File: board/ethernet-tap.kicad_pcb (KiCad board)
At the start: 4 copper layers, 399 parts, among them J1 BARREL_JACK, J10 XILINX_JTAG, J2 BEL_FUSE_0826-1G1T-23-F, J3 JUMPER_0402_SPDT, J4 JUMPER_0402_SPDT, J5 RJ45, J6 BEL_FUSE_0826-1G1T-23-F, J7 BEL_FUSE_0826-1G1T-23-F, J8 BEL_FUSE_0826-1G1T-23-F, J9 XILINX_JTAG, SW1 SWITCH, SW2 SWITCH, SW3 SWITCH, SW4 SWITCH, SW5 SWITCH, SW6 SWITCH, SW7 BUTTON, U1 LTC3374-QFN, U10 ECS-2016MVQ-250-CN-TR, U11 ECS-2016MVQ-250-CN-TR, U12 ECS-2016MVQ-250-CN-TR, U13 STM32H735-UFBGA176-25, U14 S25FLxxxS_BGA24_5x5_VIO, U2 KSZ9031RN, U3 MAX232, U4 XC7S15-1FTGB196C, U5 KSZ9031RN, U6 KSZ9031RN, U7 ECS-2016MVQ-250-CN-TR, U8 ECS-2016MVQ-250-CN-TR, U9 KSZ9031RN

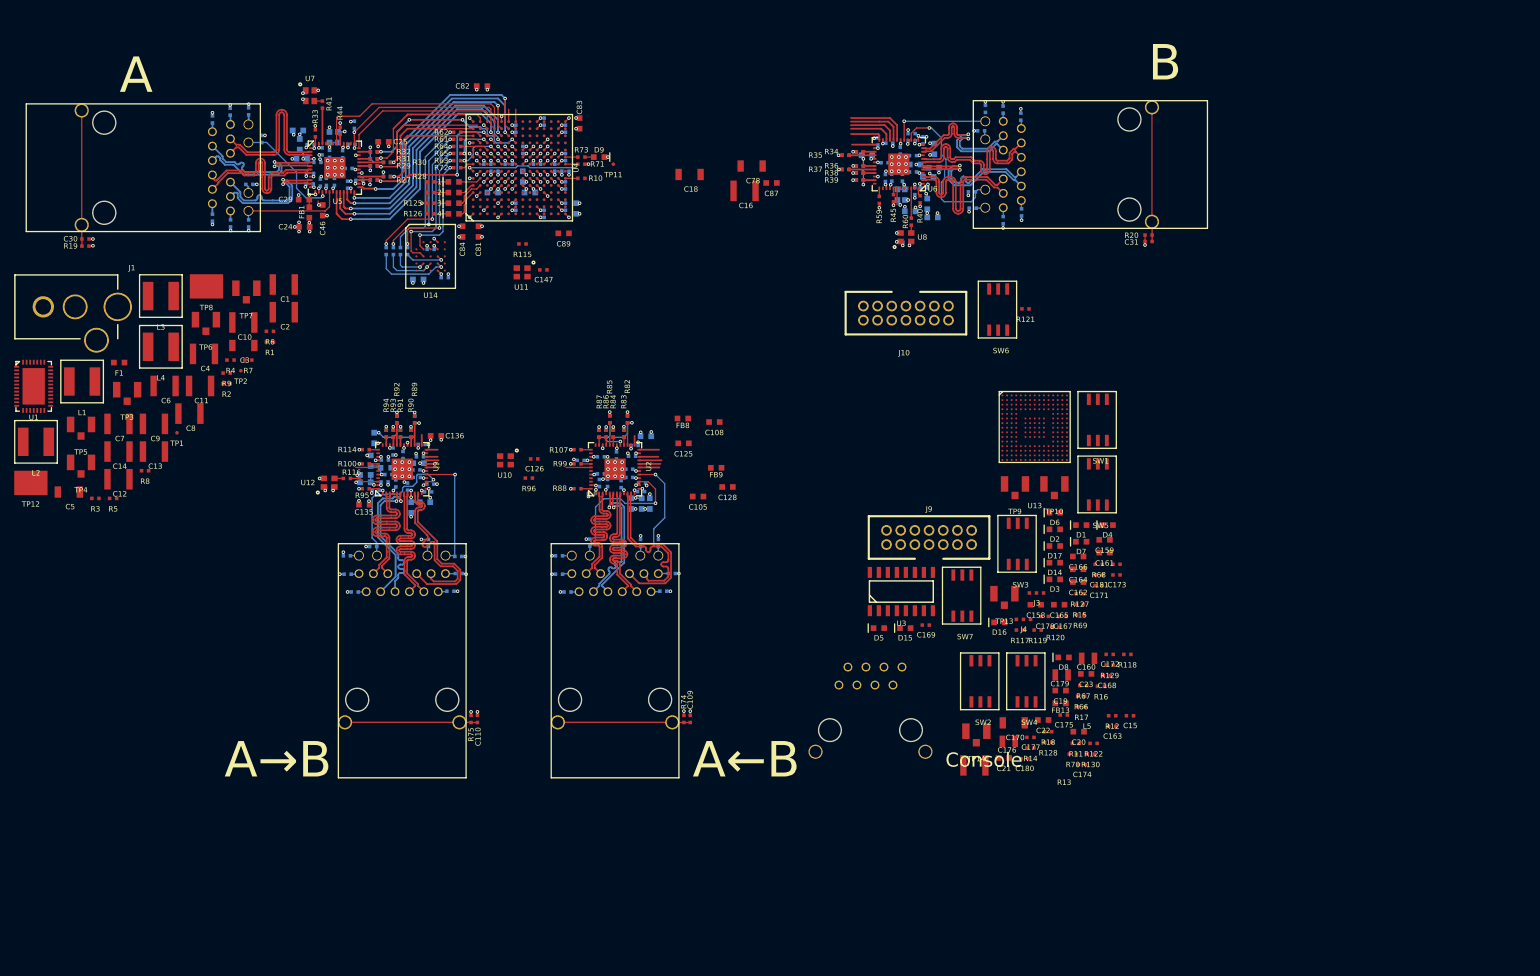
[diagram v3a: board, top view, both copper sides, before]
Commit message: Shrunk board down to 139 x 92 mm
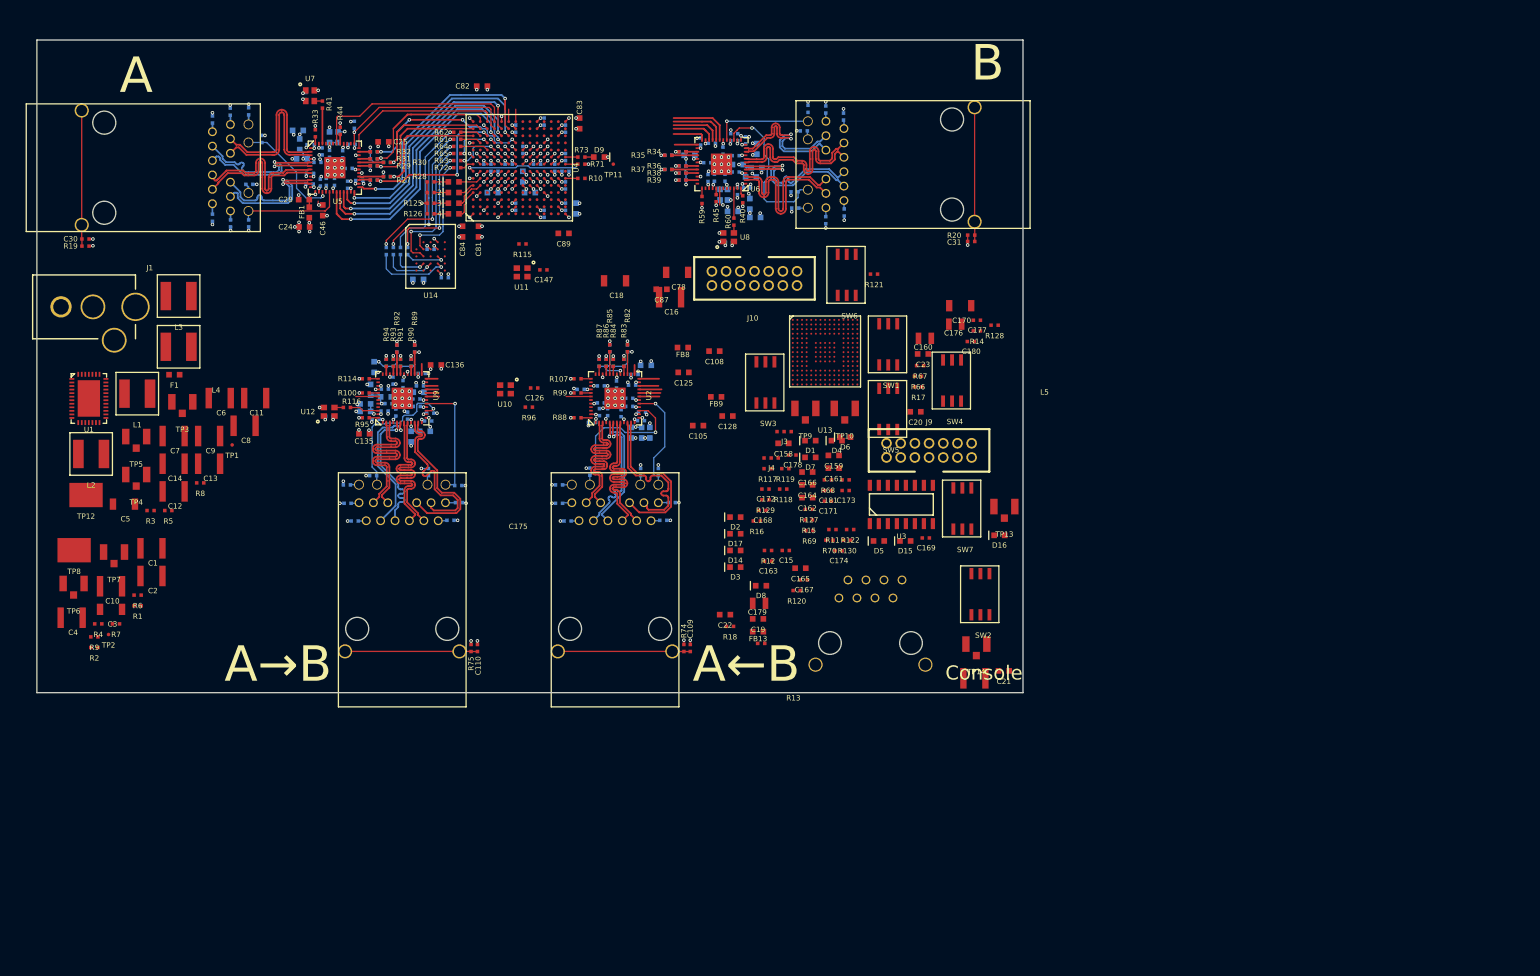
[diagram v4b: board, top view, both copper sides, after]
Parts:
- moved C176 59.3 mm to (150.4, 61.0)
- moved C177 59.3 mm to (153.5, 60.5)
- moved R128 59.3 mm to (156.0, 61.2)
- moved R14 59.3 mm to (153.5, 62.0)
- moved C180 59.3 mm to (152.7, 63.5)
- moved C170 59.3 mm to (151.2, 58.4)
- moved C15 53.8 mm to (126.6, 93.0)
- moved C163 53.8 mm to (124.1, 94.5)
- moved C168 53.8 mm to (123.3, 87.3)
- moved R12 53.8 mm to (124.1, 93.0)
- moved C172 53.8 mm to (123.7, 84.3)
- moved R118 53.8 mm to (126.2, 84.3)
- moved R129 53.8 mm to (123.7, 85.8)
- moved R16 53.8 mm to (122.5, 88.8)
- moved C160 50.6 mm to (146.2, 63.0)
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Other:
- board outline added: 139 x 92 mm

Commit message: Finished power supply layout, added mounting holes and a bunch of silkscreen labeling
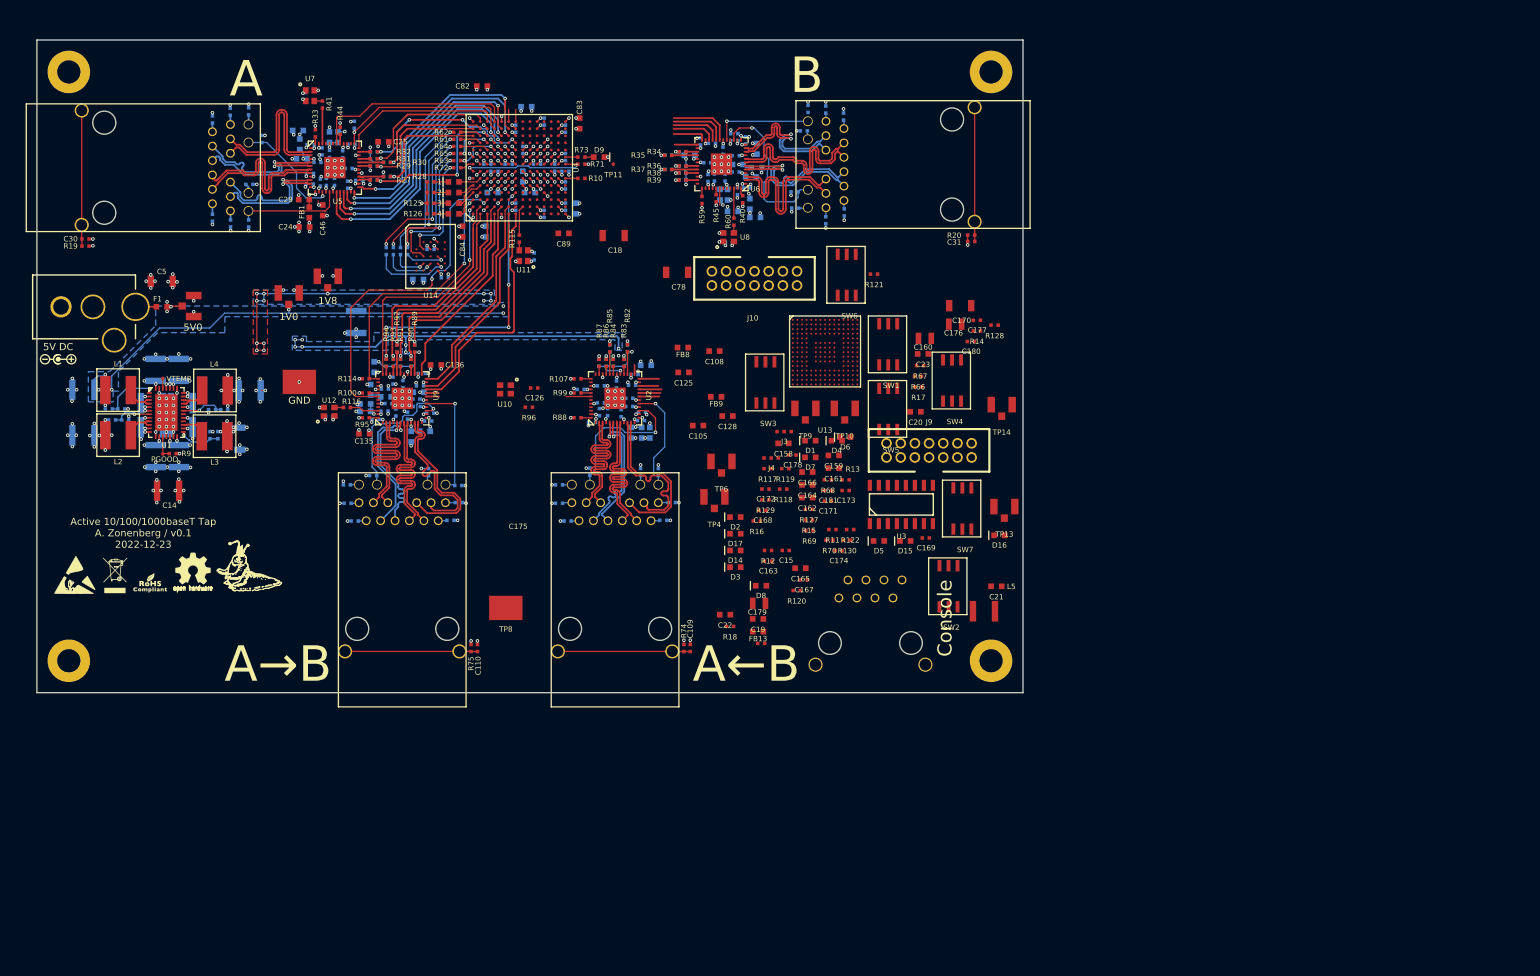
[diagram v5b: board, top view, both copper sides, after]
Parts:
- added G***: LOGO, w_logo:Logo_silk_OSHW_6x6mm, F.Cu at (43.0, 95.5)
- added G***: LOGO, azonenberg_pcb:LONGTHING-1200DPI, F.Cu at (51.5, 95.5)
- added G***: LOGO, w_logo:Logo_silk_ROHS_5x2.8mm, F.Cu at (37.0, 97.5)
- added G***: LOGO, w_logo:Logo_silk_WEEE_3.4x5mm, F.Cu at (32.0, 96.5)
- added G***: LOGO, azonenberg_pcb:LOGO_ESD_SENSITIVE_7MM, F.Cu at (26.5, 96.5)
- added G***: LOGO, w_logo:Logo_silk_polarity_center_5x1.4mm, F.Cu at (24.0, 66.0)
- added MH1: HOLE, azonenberg_pcb:MECHANICAL_CLEARANCEHOLE_4_40, F.Cu at (25.5, 25.5)
- added MH2: HOLE, azonenberg_pcb:MECHANICAL_CLEARANCEHOLE_4_40, F.Cu at (155.5, 25.5)
- added MH3: HOLE, azonenberg_pcb:MECHANICAL_CLEARANCEHOLE_4_40, F.Cu at (155.5, 108.5)
- added MH4: HOLE, azonenberg_pcb:MECHANICAL_CLEARANCEHOLE_4_40, F.Cu at (25.5, 108.5)
- C1, C10, C11, C12, C13, C147, C16, C2, C3, C4, C6, C7, C8, C81, C87, C9, R1, R2, R3, R4, R5, R6, R7, R8: moved to B.Cu
- moved TP6 92.9 mm to (117.5, 80.5)
- moved TP4 81.6 mm to (116.5, 85.5)
- moved TP8 61.4 mm to (87.1, 101.0)
- moved C16 44.4 mm to (66.0, 60.8), turned to -90 degrees
- moved TP7 44.1 mm to (56.5, 56.8)
- moved C4 40.7 mm to (51.0, 70.4)
- moved TP2 36.9 mm to (38.8, 68.7)
- moved TP5 35.2 mm to (62.0, 54.4)
- moved TP12 34.0 mm to (58.0, 69.2)
- moved TP14 33.9 mm to (157.0, 72.5)
- moved R2 33.8 mm to (32.9, 73.0), turned to 180 degrees
- moved R7 33.8 mm to (47.4, 73.1)
- moved C87 32.0 mm to (90.0, 30.4), turned to 180 degrees
- moved C10 31.9 mm to (41.0, 67.5), turned to 90 degrees
- moved C5 31.9 mm to (38.6, 55.0)
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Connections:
- U4 pad A2: unconnected-(U4-PadA2) -> /Monitor Path/ETH3_MDC
- U4 pad A3: unconnected-(U4-PadA3) -> /Monitor Path/ETH3_MDIO
- U4 pad B1: unconnected-(U4-PadB1) -> /Monitor Path/ETH3_RGMII_RXD0
- U4 pad B2: unconnected-(U4-PadB2) -> /Monitor Path/ETH3_RGMII_RX_DV
- U4 pad C1: /Monitor Path/ETH3_RGMII_RX_DV -> /Monitor Path/ETH3_RGMII_RXD1
- U4 pad C3: unconnected-(U4-PadC3) -> /Monitor Path/ETH3_RST_N
- U4 pad D1: /Monitor Path/ETH3_RGMII_RXD0 -> /Monitor Path/ETH3_RGMII_RXD3
- U4 pad D2: /Monitor Path/ETH3_RGMII_RXD1 -> /Monitor Path/ETH3_RGMII_RXD2
- U4 pad E2: /Monitor Path/ETH3_RGMII_RXD2 -> /Monitor Path/ETH3_RGMII_TX_EN
- U4 pad F1: unconnected-(U4-PadF1) -> /Monitor Path/ETH3_RGMII_TXD3
- U4 pad F2: unconnected-(U4-PadF2) -> /Monitor Path/ETH3_RGMII_TX_CLK
- U4 pad F4: /Monitor Path/ETH3_MDIO -> unconnected-(U4-PadF4)
- U4 pad G1: unconnected-(U4-PadG1) -> /Monitor Path/ETH3_RGMII_TXD2
- U4 pad G4: /Monitor Path/ETH2_RGMII_RX_CLK -> /Monitor Path/ETH3_RGMII_RX_CLK
- U4 pad H1: /Monitor Path/ETH3_RST_N -> unconnected-(U4-PadH1)
- U4 pad H3: /Monitor Path/ETH3_MDC -> unconnected-(U4-PadH3)
- U4 pad H4: /Monitor Path/ETH3_RGMII_RX_CLK -> /Monitor Path/ETH2_RGMII_RX_CLK
- U4 pad J3: /Monitor Path/ETH3_RGMII_TX_EN -> unconnected-(U4-PadJ3)
- U4 pad J4: /Monitor Path/ETH3_RGMII_TX_CLK -> unconnected-(U4-PadJ4)
- U4 pad K3: /Monitor Path/ETH3_RGMII_TXD3 -> unconnected-(U4-PadK3)
- U4 pad K4: /Monitor Path/ETH3_RGMII_TXD2 -> unconnected-(U4-PadK4)
- U4 pad M1: /Monitor Path/ETH3_RGMII_RXD3 -> unconnected-(U4-PadM1)
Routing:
- net /GND: track 750.4 -> 975.7 mm, vias 207 -> 278
- net /5V0: track 0.00 -> 161.4 mm, vias 0 -> 36
- net /1V2: track 114.6 -> 242.4 mm, vias 34 -> 49
- net /3V3: track 417.5 -> 519.4 mm, vias 70 -> 80
- net /1V8: track 39.5 -> 127.0 mm, vias 7 -> 27
- net /1V0: track 50.8 -> 133.4 mm, vias 13 -> 20
- net /Monitor Path/ETH3_RST_N: track 3.15 -> 47.3 mm, vias 0 -> 2
- net /Monitor Path/ETH3_RGMII_RX_CLK: track 1.00 -> 41.7 mm, vias 1 -> 5
- net /Monitor Path/ETH3_MDIO: track 1.25 -> 36.8 mm, vias 0 -> 2
- net /Monitor Path/ETH3_MDC: track 0.00 -> 33.1 mm, vias 0 -> 2
- net /Monitor Path/ETH3_RGMII_TXD2: track 1.70 -> 34.5 mm
- net /Monitor Path/ETH3_RGMII_RX_DV: track 0.98 -> 30.4 mm
- net /Monitor Path/ETH3_RGMII_RXD2: track 0.98 -> 29.4 mm
- net /Monitor Path/ETH3_RGMII_TX_CLK: track 1.60 -> 30.0 mm
- net /Monitor Path/ETH3_RGMII_TXD3: track 1.60 -> 30.0 mm
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- added copper zone on B.Cu, net /1V0
- added copper zone on B.Cu, net /1V2
- added copper zone on B.Cu, net /1V8
- added copper zone on F.Cu, net /1V8
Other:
- board text added: "1V0"
- board text added: "1V8"
- board text added: "5V DC"
- board text added: "5V0"
- board text added: "Active 10/100/1000baseT Tap A. Zonenberg / v0.1 2022-12-23"
- board text added: "GND"
- board text added: "PGOOD"
- board text added: "VTEMP"

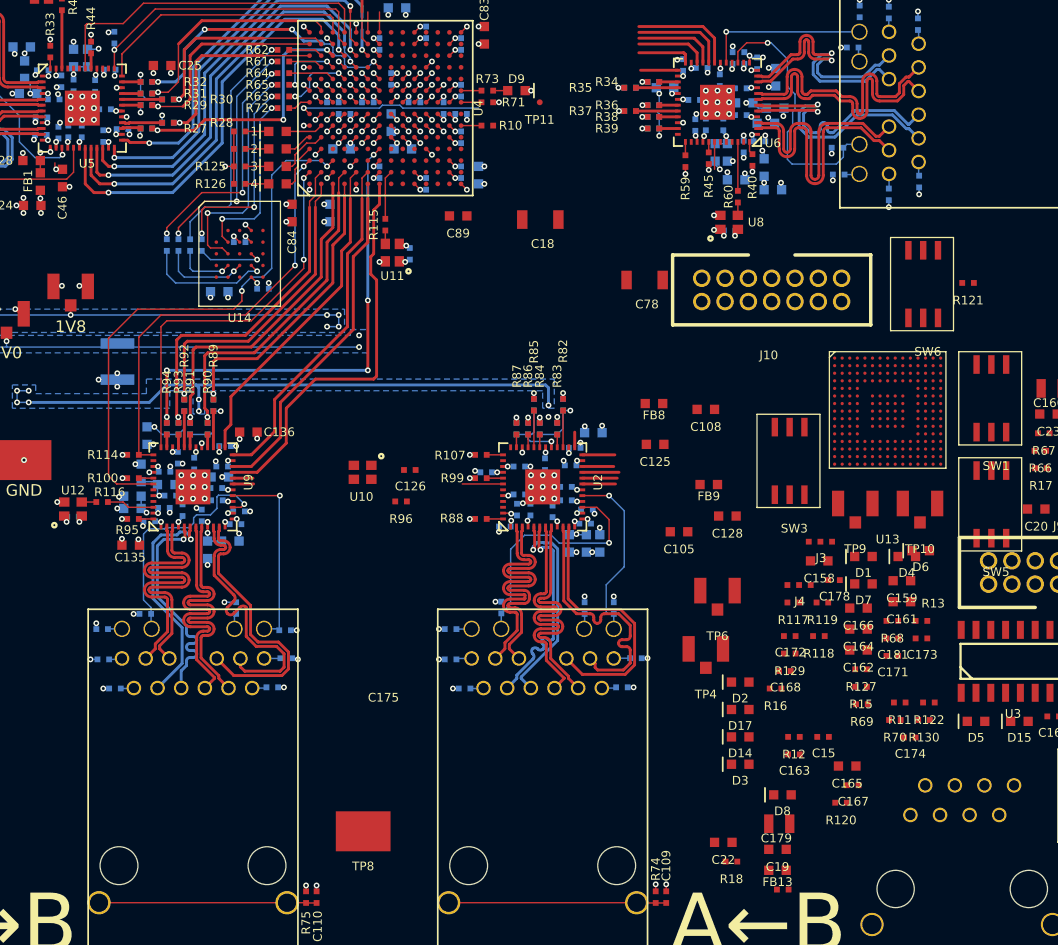
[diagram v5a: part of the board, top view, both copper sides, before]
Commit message: Continued work on layout. Monitor port PHys are now done, as is FPGA JTAG and reset
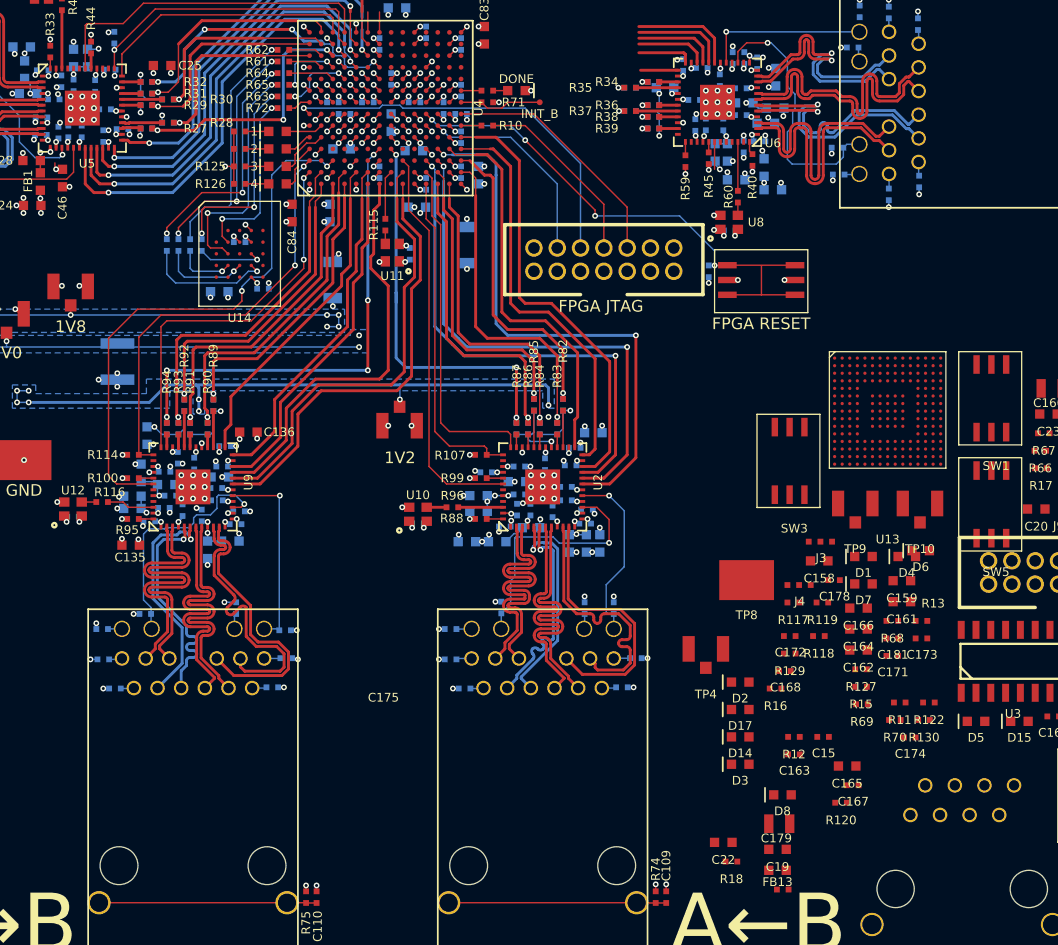
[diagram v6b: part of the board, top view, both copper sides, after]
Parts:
- C105, C108, C125, C126, C128, C18, C78, C89, FB8, FB9, R121: moved to B.Cu
- moved TP8 39.3 mm to (120.0, 79.5)
- moved TP6 30.8 mm to (90.2, 66.2), turned to 180 degrees
- moved R121 22.3 mm to (116.8, 53.0), turned to -90 degrees
- moved C128 21.4 mm to (97.0, 73.6), turned to 180 degrees
- moved FB9 19.8 mm to (97.0, 72.2)
- moved C18 18.5 mm to (84.5, 53.8), turned to 90 degrees
- moved C105 18.2 mm to (96.0, 76.2), turned to 180 degrees
- moved C108 18.1 mm to (101.5, 75.0)
- moved FB8 17.9 mm to (98.6, 76.2)
- moved C78 15.5 mm to (96.0, 50.8), turned to -90 degrees
- moved J10 14.6 mm to (107.8, 52.0), turned to 0 degrees
- moved SW6 13.9 mm to (121.2, 53.8), turned to 90 degrees
- moved C125 12.3 mm to (100.3, 71.0)
- moved U10 5.96 mm to (91.8, 73.8), turned to 180 degrees
- moved C126 4.60 mm to (91.8, 74.6)
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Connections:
- U4 pad J1: /Monitor Path/ETH3_RGMII_TXD1 -> /Monitor Path/ETH3_RGMII_TXD0
- U4 pad J2: /Monitor Path/ETH3_RGMII_TXD0 -> /Monitor Path/ETH3_RGMII_TXD1
- U4 pad J3: unconnected-(U4-PadJ3) -> /Monitor Path/ETH2_RST_N
- U4 pad L1: /Monitor Path/ETH2_RGMII_TXD0 -> /Monitor Path/ETH2_MDIO
- U4 pad L2: /Monitor Path/ETH2_RGMII_RXD1 -> /Monitor Path/ETH2_MDC
- U4 pad L3: /Monitor Path/ETH2_RGMII_RXD2 -> /Monitor Path/ETH2_RGMII_TXD2
- U4 pad L5: /Monitor Path/ETH2_RST_N -> unconnected-(U4-PadL5)
- U4 pad M1: unconnected-(U4-PadM1) -> /Monitor Path/ETH2_RGMII_RX_DV
- U4 pad M2: /Monitor Path/ETH2_RGMII_TXD2 -> /Monitor Path/ETH2_RGMII_RXD0
- U4 pad M4: /Monitor Path/ETH2_RGMII_RX_DV -> /Monitor Path/ETH2_RGMII_TXD0
- U4 pad M5: /Monitor Path/ETH2_RGMII_RXD0 -> unconnected-(U4-PadM5)
- U4 pad N1: /Monitor Path/ETH2_RGMII_TX_CLK -> /Monitor Path/ETH2_RGMII_RXD1
- U4 pad N4: /Monitor Path/ETH2_MDIO -> /Monitor Path/ETH2_RGMII_TX_EN
- U4 pad P2: /Monitor Path/ETH2_RGMII_TXD3 -> /Monitor Path/ETH2_RGMII_RXD2
- U4 pad P4: /Monitor Path/ETH2_RGMII_TX_EN -> /Monitor Path/ETH2_RGMII_TX_CLK
- U4 pad P5: /Monitor Path/ETH2_MDC -> /Monitor Path/ETH2_RGMII_TXD3
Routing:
- net /5V0: track 161.4 -> 243.5 mm
- net /GND: track 975.7 -> 1037.0 mm, vias 278 -> 288
- net /FPGA Support/FPGA_RST_N: track 0.71 -> 46.4 mm, vias 1 -> 4
- net /Monitor Path/ETH2_RGMII_TXD0: track 2.85 -> 47.7 mm, vias 0 -> 2
- net /Monitor Path/ETH2_RGMII_TXD1: track 3.00 -> 44.7 mm, vias 0 -> 2
- net /Monitor Path/ETH2_RGMII_TXD2: track 3.15 -> 43.1 mm, vias 0 -> 2
- net /Monitor Path/ETH3_RGMII_TXD1: track 1.75 -> 38.4 mm
- net /Monitor Path/ETH3_RGMII_TXD0: track 1.80 -> 38.2 mm
- net /Monitor Path/ETH2_RGMII_TXD3: track 2.70 -> 38.2 mm
- net /3V3: track 519.4 -> 554.3 mm, vias 80 -> 85
- net /Monitor Path/ETH2_RGMII_RX_CLK: track 0.90 -> 34.8 mm, vias 1 -> 3
- net /Monitor Path/ETH2_RGMII_TX_EN: track 1.30 -> 33.6 mm
- net /Monitor Path/ETH2_RGMII_TX_CLK: track 2.80 -> 34.9 mm
- net /Monitor Path/ETH2_RST_N: track 3.50 -> 34.2 mm
- net /Monitor Path/ETH2_MDC: track 0.00 -> 29.5 mm
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- added copper zone on In2.Cu, net /5V0
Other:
- board text added: "1V2"
- board text added: "DONE"
- board text added: "FPGA JTAG"
- board text added: "FPGA RESET"
- board text added: "INIT_B"
